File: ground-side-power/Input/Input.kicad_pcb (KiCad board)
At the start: 2 copper layers, 95.8 x 122.1 mm, 41 parts, among them J1 Battery Terminals, J2 Battery Terminals, J26 Conn_01x02_Female, J3 Battery Terminals, J4 Battery Terminals, J5 874270842, J6 874270842, J7 ATX-24, J8 Conn_01x03_Female, J9 Conn_01x03_Female, K1 AZ2150-1A-12DEF, M1 Fan_PC_Chassis, SW1 GRB234A2NABA1, U1 INA180, U2 INA180

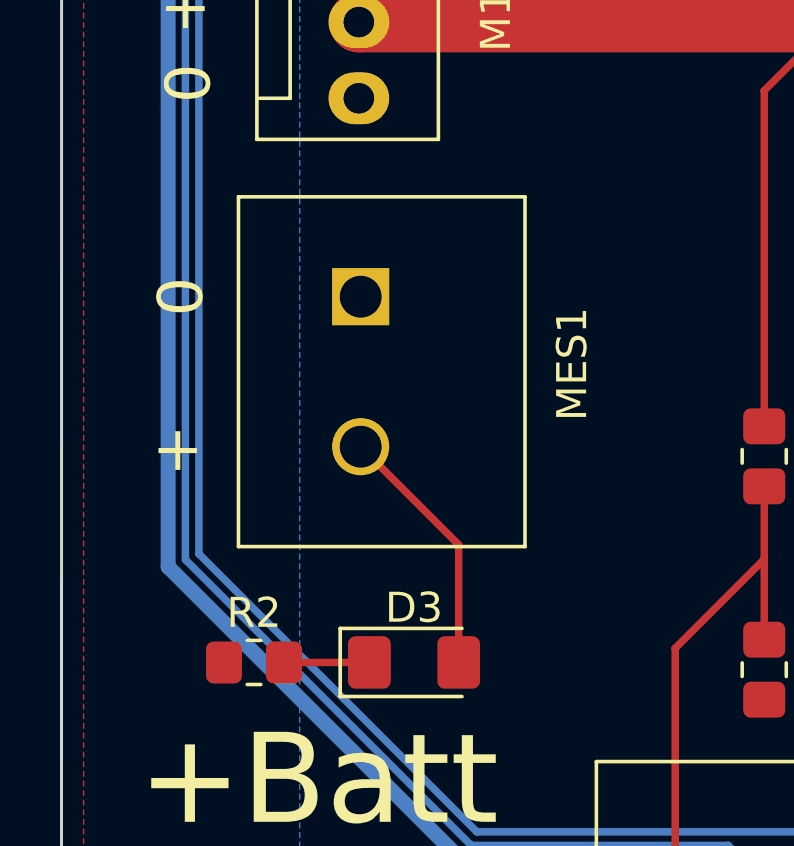
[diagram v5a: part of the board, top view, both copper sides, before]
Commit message: Fixed footprint issue
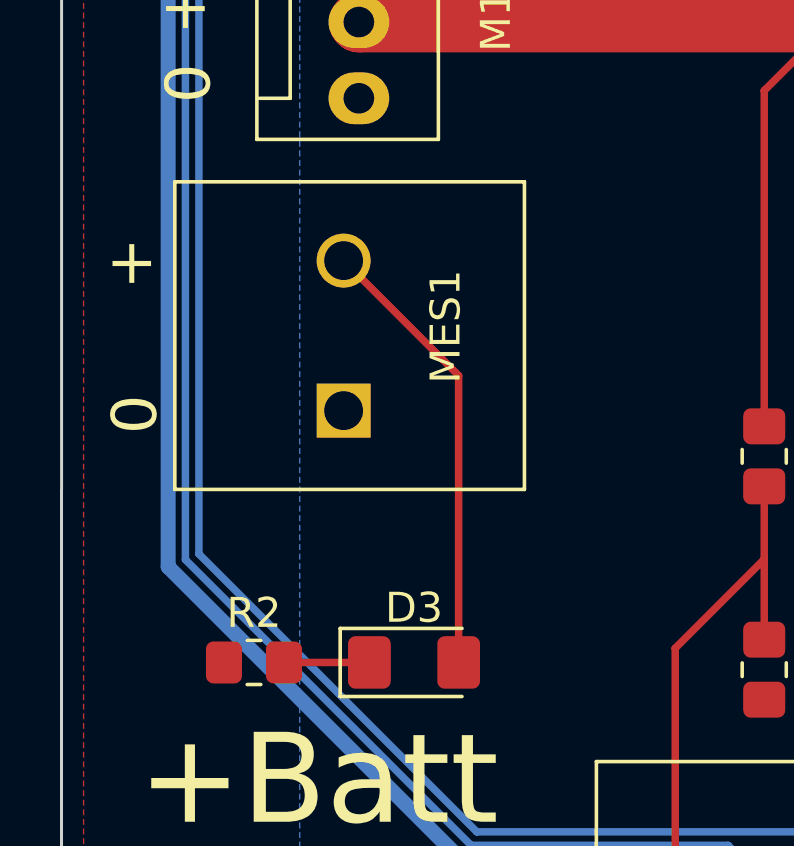
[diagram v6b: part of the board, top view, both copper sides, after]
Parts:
- MES1: footprint GSP:OSTTA020161 -> GSP:1935310
- moved MES1 3.84 mm to (107.4, 133.2), turned to 90 degrees
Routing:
- net +BATT: track 16.8 -> 23.3 mm
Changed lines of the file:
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@@
     )
   )
-  (footprint "GSP:OSTTA020161" (layer "F.Cu")
-    (at 107.96 129.426 -90)
+  (footprint "GSP:1935310" (layer "F.Cu")
+    (at 107.391799 133.223 90)
     (property "Sheetfile" "Input.kicad_sch")
     (property "Sheetname" "")
     (attr through_hole)
-    (fp_text reference "MES1" (at 2.246 -7.051799 -90) (layer "F.SilkS")
-      (effects (font (size 1 1) (thickness 0.15)))
-    )
-    (fp_text value "PRT-14313" (at 5.33 2.4 90) (layer "F.SilkS") hide
-      (effects (font (size 1 1) (thickness 0.15)))
-    )
-    (fp_text user "Front" (at 0 1.8 -90 unlocked) (layer "Cmts.User") hide
-      (effects (font (size 1 1) (thickness 0.15)))
-    )
-    (fp_text user "*" (at 2.63 0 90) (layer "F.Fab") hide
-      (effects (font (size 1 1) (thickness 0.15)))
-    )
-    (fp_line (start 8.3293 -5.476999) (end -3.3293 -5.476999) (layer "F.SilkS") (width 0.12))
-    (fp_line (start 8.3293 4.073401) (end 8.3293 -5.476999) (layer "F.SilkS") (width 0.12))
-    (fp_line (start -3.3293 -5.476999) (end -3.3293 4.073401) (layer "F.SilkS") (width 0.12))
-    (fp_line (start -3.3293 4.073401) (end 8.3293 4.073401) (layer "F.SilkS") (width 0.12))
-    (fp_line (start 8.4563 -5.603999) (end -3.4563 -5.603999) (layer "F.CrtYd") (width 0.05))
-    (fp_line (start 8.4563 4.200401) (end 8.4563 -5.603999) (layer "F.CrtYd") (width 0.05))
-    (fp_line (start -3.4563 4.200401) (end 8.4563 4.200401) (layer "F.CrtYd") (width 0.05))
-    (fp_line (start -3.4563 -5.603999) (end -3.4563 4.200401) (layer "F.CrtYd") (width 0.05))
-    (fp_line (start -3.4563 4.200401) (end 8.4563 4.200401) (layer "F.CrtYd") (width 0.05))
-    (fp_line (start 8.4563 4.200401) (end 8.4563 -5.603999) (layer "F.CrtYd") (width 0.05))
-    (fp_line (start 8.4563 -5.603999) (end -3.4563 -5.603999) (layer "F.CrtYd") (width 0.05))
-    (fp_line (start -3.4563 -5.603999) (end -3.4563 4.200401) (layer "F.CrtYd") (width 0.05))
-    (fp_line (start 8.2023 3.946401) (end 8.2023 -5.349999) (layer "F.Fab") (width 0.1))
-    (fp_line (start -3.2023 -5.349999) (end -3.2023 3.946401) (layer "F.Fab") (width 0.1))
-    (fp_line (start -3.2023 3.946401) (end 8.2023 3.946401) (layer "F.Fab") (width 0.1))
-    (fp_line (start 8.2023 -5.349999) (end -3.2023 -5.349999) (layer "F.Fab") (width 0.1))
-    (pad "1" thru_hole rect (at 0 0 270) (size 1.905 1.905) (drill 1.397) (layers *.Cu *.Mask)
+    (fp_text reference "MES1" (at 2.8 3.4 90) (layer "F.SilkS")
+      (effects (font (size 1 1) (thickness 0.15)))
+    )
+    (fp_text value "PRT-14313" (at 2.3 -6.7 90) (layer "F.SilkS") hide
+      (effects (font (size 1 1) (thickness 0.15)))
+    )
+    (fp_text user "FRONT" (at 2.5 -2.9 90 unlocked) (layer "Cmts.User") hide
+      (effects (font (size 1 1) (thickness 0.15)))
+    )
+    (fp_text user "*" (at 0 0 90) (layer "F.Fab") hide
+      (effects (font (size 1 1) (thickness 0.15)))
+    )
+    (fp_line (start 7.627 6.027001) (end 7.627 -5.626999) (layer "F.SilkS") (width 0.12))
+    (fp_line (start -2.627 -5.626999) (end -2.627 6.027001) (layer "F.SilkS") (width 0.12))
+    (fp_line (start 7.627 -5.626999) (end -2.627 -5.626999) (layer "F.SilkS") (width 0.12))
+    (fp_line (start -2.627 6.027001) (end 7.627 6.027001) (layer "F.SilkS") (width 0.12))
+    (fp_line (start 7.754 6.154001) (end 7.754 -5.753999) (layer "F.CrtYd") (width 0.05))
+    (fp_line (start -2.754 6.154001) (end 7.754 6.154001) (layer "F.CrtYd") (width 0.05))
+    (fp_line (start -2.754 -5.753999) (end -2.754 6.154001) (layer "F.CrtYd") (width 0.05))
+    (fp_line (start 7.754 -5.753999) (end -2.754 -5.753999) (layer "F.CrtYd") (width 0.05))
+    (fp_line (start 7.754 -5.753999) (end -2.754 -5.753999) (layer "F.CrtYd") (width 0.05))
+    (fp_line (start -2.754 -5.753999) (end -2.754 6.154001) (layer "F.CrtYd") (width 0.05))
+    (fp_line (start -2.754 6.154001) (end 7.754 6.154001) (layer "F.CrtYd") (width 0.05))
+    (fp_line (start 7.754 6.154001) (end 7.754 -5.753999) (layer "F.CrtYd") (width 0.05))
+    (fp_line (start -2.5 -5.499999) (end -2.5 5.900001) (layer "F.Fab") (width 0.1))
+    (fp_line (start 7.5 5.900001) (end 7.5 -5.499999) (layer "F.Fab") (width 0.1))
+    (fp_line (start -2.5 5.900001) (end 7.5 5.900001) (layer "F.Fab") (width 0.1))
+    (fp_line (start 7.5 -5.499999) (end -2.5 -5.499999) (layer "F.Fab") (width 0.1))
+    (pad "1" thru_hole rect (at 0 0 90) (size 1.8034 1.8034) (drill 1.2954) (layers *.Cu *.Mask)
       (net 2 "GND") (pinfunction "-") (pintype "passive"))
-    (pad "2" thru_hole circle (at 5 0 270) (size 1.905 1.905) (drill 1.397) (layers *.Cu *.Mask)
+    (pad "2" thru_hole circle (at 5 0 90) (size 1.8034 1.8034) (drill 1.2954) (layers *.Cu *.Mask)
       (net 1 "+BATT") (pinfunction "+") (pintype "passive"))
   )
@@
   (gr_line (start 100.781656 160.274) (end 191.008044 160.274) (layer "Edge.Cuts") (width 0.1))
   (gr_line (start 193.802044 157.48) (end 193.812044 40.977656) (layer "Edge.Cuts") (width 0.1))
-  (gr_text "0" (at 101.864 129.426 270) (layer "F.SilkS")
+  (gr_text "0" (at 100.33 133.35 270) (layer "F.SilkS")
     (effects (font (size 1.5 1.5) (thickness 0.3)))
   )
@@
     (effects (font (size 0.75 0.75) (thickness 0.1875)))
   )
-  (gr_text "+" (at 101.864 134.506) (layer "F.SilkS")
+  (gr_text "+" (at 100.33 128.27) (layer "F.SilkS")
     (effects (font (size 1.5 1.5) (thickness 0.3)))
   )
@@
     (effects (font (size 1.5 1.5) (thickness 0.3)))
   )
-  (segment (start 111.2255 137.6915) (end 107.96 134.426) (width 0.25) (layer "F.Cu") (net 1))
-  (segment (start 111.2255 141.618) (end 111.2255 137.6915) (width 0.25) (layer "F.Cu") (net 1))
+  (segment (start 111.2255 132.056701) (end 107.391799 128.223) (width 0.25) (layer "F.Cu") (net 1))
+  (segment (start 111.2255 141.618) (end 111.2255 132.056701) (width 0.25) (layer "F.Cu") (net 1))
   (segment (start 125.74 100.776) (end 125.74 101.996) (width 0.25) (layer "B.Cu") (net 1))
   (segment (start 125.4215 100.4575) (end 125.74 100.776) (width 0.25) (layer "B.Cu") (net 1))

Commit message: Added Gerbers
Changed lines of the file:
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@@
       (layerselection 0x00010fc_ffffffff)
       (disableapertmacros false)
-      (usegerberextensions false)
-      (usegerberattributes true)
-      (usegerberadvancedattributes true)
-      (creategerberjobfile true)
+      (usegerberextensions true)
+      (usegerberattributes false)
+      (usegerberadvancedattributes false)
+      (creategerberjobfile false)
       (svguseinch false)
       (svgprecision 6)
@@
       (psa4output false)
       (plotreference true)
-      (plotvalue true)
+      (plotvalue false)
       (plotinvisibletext false)
       (sketchpadsonfab false)
-      (subtractmaskfromsilk false)
+      (subtractmaskfromsilk true)
       (outputformat 1)
       (mirror false)
-      (drillshape 1)
+      (drillshape 0)
       (scaleselection 1)
-      (outputdirectory "")
+      (outputdirectory "../Gerbers/Input/")
     )
   )
@@
     (fp_line (start -1.2 -0.8) (end -1.6 -0.4) (layer "F.Fab") (width 0.1))
     (fp_line (start -1.6 -0.4) (end -1.6 0.8) (layer "F.Fab") (width 0.1))
-    (pad "1" smd roundrect (at -1.4875 0) (size 1.425 1.75) (layers "F.Cu" "F.Paste" "F.Mask") (roundrect_rratio 0.175439)
+    (pad "1" smd roundrect (at -1.4875 0) (size 1.425 1.75) (layers "F.Cu" "F.Paste" "F.Mask") (roundrect_rratio 0.1754392982)
       (net 7 "Net-(D3-Pad1)") (pinfunction "K") (pintype "passive"))
-    (pad "2" smd roundrect (at 1.4875 0) (size 1.425 1.75) (layers "F.Cu" "F.Paste" "F.Mask") (roundrect_rratio 0.175439)
+    (pad "2" smd roundrect (at 1.4875 0) (size 1.425 1.75) (layers "F.Cu" "F.Paste" "F.Mask") (roundrect_rratio 0.1754392982)
       (net 1 "+BATT") (pinfunction "A") (pintype "passive"))
     (model "${KICAD6_3DMODEL_DIR}/Diode_SMD.3dshapes/D_1206_3216Metric.wrl"
@@
     (fp_line (start 1 0.625) (end -1 0.625) (layer "F.Fab") (width 0.1))
     (fp_line (start -1 -0.625) (end 1 -0.625) (layer "F.Fab") (width 0.1))
-    (pad "1" smd roundrect (at -1 0 90) (size 1.2 1.4) (layers "F.Cu" "F.Paste" "F.Mask") (roundrect_rratio 0.208333)
+    (pad "1" smd roundrect (at -1 0 90) (size 1.2 1.4) (layers "F.Cu" "F.Paste" "F.Mask") (roundrect_rratio 0.2083333333)
       (net 2 "GND") (pintype "passive"))
-    (pad "2" smd roundrect (at 1 0 90) (size 1.2 1.4) (layers "F.Cu" "F.Paste" "F.Mask") (roundrect_rratio 0.208333)
+    (pad "2" smd roundrect (at 1 0 90) (size 1.2 1.4) (layers "F.Cu" "F.Paste" "F.Mask") (roundrect_rratio 0.2083333333)
       (net 8 "Net-(D4-Pad1)") (pintype "passive"))
     (model "${KICAD6_3DMODEL_DIR}/Resistor_SMD.3dshapes/R_0805_2012Metric.wrl"
@@
     (fp_line (start -1 0.625) (end -1 -0.625) (layer "F.Fab") (width 0.1))
     (fp_line (start 1 0.625) (end -1 0.625) (layer "F.Fab") (width 0.1))
-    (pad "1" smd roundrect (at -1 0 270) (size 1.2 1.4) (layers "F.Cu" "F.Paste" "F.Mask") (roundrect_rratio 0.208333)
+    (pad "1" smd roundrect (at -1 0 270) (size 1.2 1.4) (layers "F.Cu" "F.Paste" "F.Mask") (roundrect_rratio 0.2083333333)
       (net 3 "+12V") (pintype "passive"))
-    (pad "2" smd roundrect (at 1 0 270) (size 1.2 1.4) (layers "F.Cu" "F.Paste" "F.Mask") (roundrect_rratio 0.208333)
+    (pad "2" smd roundrect (at 1 0 270) (size 1.2 1.4) (layers "F.Cu" "F.Paste" "F.Mask") (roundrect_rratio 0.2083333333)
       (net 22 "/12_VOLTAGE") (pintype "passive"))
     (model "${KICAD6_3DMODEL_DIR}/Resistor_SMD.3dshapes/R_0805_2012Metric.wrl"
@@
     (fp_line (start 1.6 0.8) (end 1.6 -0.8) (layer "F.Fab") (width 0.1))
     (fp_line (start -1.2 -0.8) (end -1.6 -0.4) (layer "F.Fab") (width 0.1))
-    (pad "1" smd roundrect (at -1.4875 0 90) (size 1.425 1.75) (layers "F.Cu" "F.Paste" "F.Mask") (roundrect_rratio 0.175439)
+    (pad "1" smd roundrect (at -1.4875 0 90) (size 1.425 1.75) (layers "F.Cu" "F.Paste" "F.Mask") (roundrect_rratio 0.1754392982)
       (net 8 "Net-(D4-Pad1)") (pinfunction "K") (pintype "passive"))
-    (pad "2" smd roundrect (at 1.4875 0 90) (size 1.425 1.75) (layers "F.Cu" "F.Paste" "F.Mask") (roundrect_rratio 0.175439)
+    (pad "2" smd roundrect (at 1.4875 0 90) (size 1.425 1.75) (layers "F.Cu" "F.Paste" "F.Mask") (roundrect_rratio 0.1754392982)
       (net 3 "+12V") (pinfunction "A") (pintype "passive"))
     (model "${KICAD6_3DMODEL_DIR}/Diode_SMD.3dshapes/D_1206_3216Metric.wrl"
@@
     (fp_line (start -1 0.625) (end -1 -0.625) (layer "F.Fab") (width 0.1))
     (fp_line (start 1 -0.625) (end 1 0.625) (layer "F.Fab") (width 0.1))
-    (pad "1" smd roundrect (at -1 0) (size 1.2 1.4) (layers "F.Cu" "F.Paste" "F.Mask") (roundrect_rratio 0.208333)
+    (pad "1" smd roundrect (at -1 0) (size 1.2 1.4) (layers "F.Cu" "F.Paste" "F.Mask") (roundrect_rratio 0.2083333333)
       (net 3 "+12V") (pintype "passive"))
-    (pad "2" smd roundrect (at 1 0) (size 1.2 1.4) (layers "F.Cu" "F.Paste" "F.Mask") (roundrect_rratio 0.208333)
+    (pad "2" smd roundrect (at 1 0) (size 1.2 1.4) (layers "F.Cu" "F.Paste" "F.Mask") (roundrect_rratio 0.2083333333)
       (net 2 "GND") (pintype "passive"))
     (model "${KICAD6_3DMODEL_DIR}/Resistor_SMD.3dshapes/R_0805_2012Metric.wrl"
@@
     (fp_line (start 1 0.625) (end -1 0.625) (layer "F.Fab") (width 0.1))
     (fp_line (start 1 -0.625) (end 1 0.625) (layer "F.Fab") (width 0.1))
-    (pad "1" smd roundrect (at -1 0 270) (size 1.2 1.4) (layers "F.Cu" "F.Paste" "F.Mask") (roundrect_rratio 0.208333)
+    (pad "1" smd roundrect (at -1 0 270) (size 1.2 1.4) (layers "F.Cu" "F.Paste" "F.Mask") (roundrect_rratio 0.2083333333)
       (net 22 "/12_VOLTAGE") (pintype "passive"))
-    (pad "2" smd roundrect (at 1 0 270) (size 1.2 1.4) (layers "F.Cu" "F.Paste" "F.Mask") (roundrect_rratio 0.208333)
+    (pad "2" smd roundrect (at 1 0 270) (size 1.2 1.4) (layers "F.Cu" "F.Paste" "F.Mask") (roundrect_rratio 0.2083333333)
       (net 2 "GND") (pintype "passive"))
     (model "${KICAD6_3DMODEL_DIR}/Resistor_SMD.3dshapes/R_0805_2012Metric.wrl"
@@
     (fp_line (start 1 -0.625) (end 1 0.625) (layer "F.Fab") (width 0.1))
     (fp_line (start 1 0.625) (end -1 0.625) (layer "F.Fab") (width 0.1))
-    (pad "1" smd roundrect (at -1 0) (size 1.2 1.4) (layers "F.Cu" "F.Paste" "F.Mask") (roundrect_rratio 0.208333)
+    (pad "1" smd roundrect (at -1 0) (size 1.2 1.4) (layers "F.Cu" "F.Paste" "F.Mask") (roundrect_rratio 0.2083333333)
       (net 2 "GND") (pintype "passive"))
-    (pad "2" smd roundrect (at 1 0) (size 1.2 1.4) (layers "F.Cu" "F.Paste" "F.Mask") (roundrect_rratio 0.208333)
+    (pad "2" smd roundrect (at 1 0) (size 1.2 1.4) (layers "F.Cu" "F.Paste" "F.Mask") (roundrect_rratio 0.2083333333)
       (net 7 "Net-(D3-Pad1)") (pintype "passive"))
     (model "${KICAD6_3DMODEL_DIR}/Resistor_SMD.3dshapes/R_0805_2012Metric.wrl"
@@
     (fp_line (start 1 0.625) (end 1 -0.625) (layer "B.Fab") (width 0.1))
     (fp_line (start 1 -0.625) (end -1 -0.625) (layer "B.Fab") (width 0.1))
-    (pad "1" smd roundrect (at -1.0375 0 270) (size 1.175 1.45) (layers "B.Cu" "B.Paste" "B.Mask") (roundrect_rratio 0.212766)
+    (pad "1" smd roundrect (at -1.0375 0 270) (size 1.175 1.45) (layers "B.Cu" "B.Paste" "B.Mask") (roundrect_rratio 0.2127659574)
       (net 2 "GND") (pintype "passive"))
-    (pad "2" smd roundrect (at 1.0375 0 270) (size 1.175 1.45) (layers "B.Cu" "B.Paste" "B.Mask") (roundrect_rratio 0.212766)
+    (pad "2" smd roundrect (at 1.0375 0 270) (size 1.175 1.45) (layers "B.Cu" "B.Paste" "B.Mask") (roundrect_rratio 0.2127659574)
       (net 4 "+5V") (pintype "passive"))
     (model "${KICAD6_3DMODEL_DIR}/Capacitor_SMD.3dshapes/C_0805_2012Metric.wrl"
@@
     (fp_line (start 1 0.625) (end 1 -0.625) (layer "B.Fab") (width 0.1))
     (fp_line (start -1 -0.625) (end -1 0.625) (layer "B.Fab") (width 0.1))
-    (pad "1" smd roundrect (at -1.0375 0 270) (size 1.175 1.45) (layers "B.Cu" "B.Paste" "B.Mask") (roundrect_rratio 0.212766)
+    (pad "1" smd roundrect (at -1.0375 0 270) (size 1.175 1.45) (layers "B.Cu" "B.Paste" "B.Mask") (roundrect_rratio 0.2127659574)
       (net 2 "GND") (pintype "passive"))
-    (pad "2" smd roundrect (at 1.0375 0 270) (size 1.175 1.45) (layers "B.Cu" "B.Paste" "B.Mask") (roundrect_rratio 0.212766)
+    (pad "2" smd roundrect (at 1.0375 0 270) (size 1.175 1.45) (layers "B.Cu" "B.Paste" "B.Mask") (roundrect_rratio 0.2127659574)
       (net 4 "+5V") (pintype "passive"))
     (model "${KICAD6_3DMODEL_DIR}/Capacitor_SMD.3dshapes/C_0805_2012Metric.wrl"
@@
     (fp_line (start -3.15 1.6) (end 3.15 1.6) (layer "B.Fab") (width 0.1))
     (fp_line (start 3.15 1.6) (end 3.15 -1.6) (layer "B.Fab") (width 0.1))
-    (pad "1" smd roundrect (at -3.05 0 270) (size 1.4 3.35) (layers "B.Cu" "B.Paste" "B.Mask") (roundrect_rratio 0.178571)
+    (pad "1" smd roundrect (at -3.05 0 270) (size 1.4 3.35) (layers "B.Cu" "B.Paste" "B.Mask") (roundrect_rratio 0.1785707143)
       (net 23 "/Sys_Sense+") (pintype "passive"))
-    (pad "2" smd roundrect (at 3.05 0 270) (size 1.4 3.35) (layers "B.Cu" "B.Paste" "B.Mask") (roundrect_rratio 0.178571)
+    (pad "2" smd roundrect (at 3.05 0 270) (size 1.4 3.35) (layers "B.Cu" "B.Paste" "B.Mask") (roundrect_rratio 0.1785707143)
       (net 1 "+BATT") (pintype "passive"))
     (model "${KICAD6_3DMODEL_DIR}/Resistor_SMD.3dshapes/R_2512_6332Metric.wrl"
@@
     (fp_line (start 3.15 1.6) (end 3.15 -1.6) (layer "B.Fab") (width 0.1))
     (fp_line (start -3.15 -1.6) (end -3.15 1.6) (layer "B.Fab") (width 0.1))
-    (pad "1" smd roundrect (at -3.05 0 270) (size 1.4 3.35) (layers "B.Cu" "B.Paste" "B.Mask") (roundrect_rratio 0.178571)
+    (pad "1" smd roundrect (at -3.05 0 270) (size 1.4 3.35) (layers "B.Cu" "B.Paste" "B.Mask") (roundrect_rratio 0.1785707143)
       (net 11 "/12V_Sense+") (pintype "passive"))
-    (pad "2" smd roundrect (at 3.05 0 270) (size 1.4 3.35) (layers "B.Cu" "B.Paste" "B.Mask") (roundrect_rratio 0.178571)
+    (pad "2" smd roundrect (at 3.05 0 270) (size 1.4 3.35) (layers "B.Cu" "B.Paste" "B.Mask") (roundrect_rratio 0.1785707143)
       (net 3 "+12V") (pintype "passive"))
     (model "${KICAD6_3DMODEL_DIR}/Resistor_SMD.3dshapes/R_2512_6332Metric.wrl"
